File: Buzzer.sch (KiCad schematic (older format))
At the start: 1 part

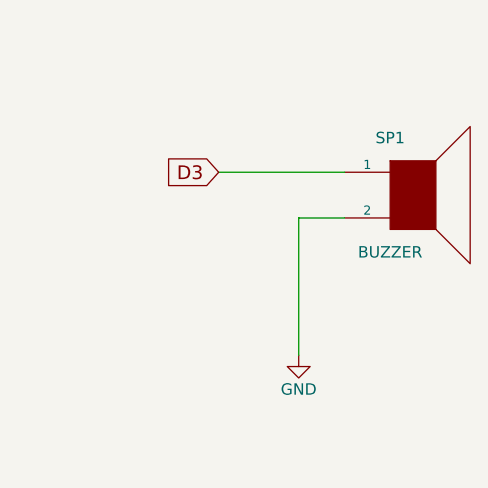
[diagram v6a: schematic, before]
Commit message: añadidos driver para led y conectores para fotodiodos infrarrojos
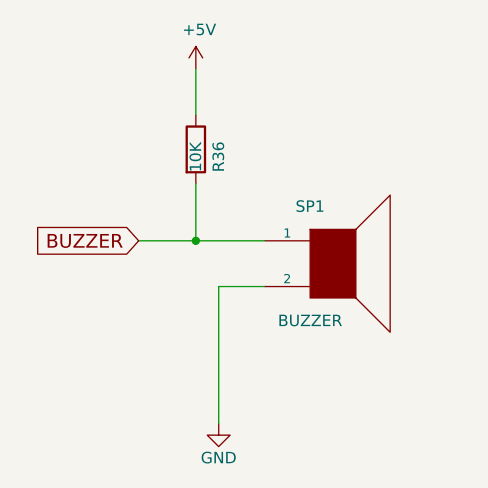
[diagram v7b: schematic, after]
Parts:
- added R36: 10K, Resistencias:R_0805, symbol R
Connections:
- net D3 renamed BUZZER
- net BUZZER: now also R36.2
- new net +5V: R36.1
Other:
- moved on the sheet: SP1
